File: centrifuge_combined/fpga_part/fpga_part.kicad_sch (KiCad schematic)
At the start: 8 parts, among them X3 EC2620TTS-100.000MTR

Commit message: Board appears ok
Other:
- title: (none) -> VGA Centrifuge
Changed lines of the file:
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@@
 (kicad_sch (version 20211123) (generator eeschema)
   (paper "A4")
+  (title_block
+    (title "VGA Centrifuge")
+    (date "2022-10-03")
+    (rev "R2")
+    (comment 1 "Author: Paolo Celati")
+    (comment 2 "FPGA Section")
+  )
   (junction (at 107.823 154.686) (diameter 0) (color 0 0 0 0)
   )

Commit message: Fixed up schematic names and page numbers
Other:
- sheet e renamed vga_dac
- sheet e1 renamed vga_adc1
- sheet e2 renamed vga_adc2
- sheet e3 renamed vga_ddc_eeprom1
- sheet e4 renamed vga_ddc_eeprom2
- sheet vga_interface renamed vga_interface3
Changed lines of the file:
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@@
     (stroke (width 0.1524) (type solid) (color 0 0 0 0))
     (fill (color 0 0 0 0.0000))
-    (property "Sheet name" "e" (id 0) (at 206.248 43.4844 0)
+    (property "Sheet name" "vga_dac" (id 0) (at 206.248 43.4844 0)
       (effects (font (size 1.27 1.27)) (justify left bottom))
     )
@@
     (stroke (width 0.1524) (type solid) (color 0 0 0 0))
     (fill (color 0 0 0 0.0000))
-    (property "Sheet name" "vga_interface" (id 0) (at 250.063 43.3574 0)
+    (property "Sheet name" "vga_interface3" (id 0) (at 250.063 43.3574 0)
       (effects (font (size 1.27 1.27)) (justify left bottom))
     )
@@
     (stroke (width 0.1524) (type solid) (color 0 0 0 0))
     (fill (color 0 0 0 0.0000))
-    (property "Sheet name" "e1" (id 0) (at 99.441 75.9964 0)
+    (property "Sheet name" "vga_adc1" (id 0) (at 99.441 75.9964 0)
       (effects (font (size 1.27 1.27)) (justify left bottom))
     )
@@
     (stroke (width 0.1524) (type solid) (color 0 0 0 0))
     (fill (color 0 0 0 0.0000))
-    (property "Sheet name" "e3" (id 0) (at 21.463 76.6314 0)
+    (property "Sheet name" "vga_ddc_eeprom1" (id 0) (at 21.463 76.6314 0)
       (effects (font (size 1.27 1.27)) (justify left bottom))
     )
@@
     (stroke (width 0.1524) (type solid) (color 0 0 0 0))
     (fill (color 0 0 0 0.0000))
-    (property "Sheet name" "e2" (id 0) (at 96.393 30.1494 0)
-      (effects (font (size 1.27 1.27)) (justify left bottom))
-    )
-    (property "Sheet file" "vga_input.kicad_sch" (id 1) (at 96.393 48.5906 0)
+    (property "Sheet name" "vga_adc2" (id 0) (at 96.393 30.1494 0)
+      (effects (font (size 1.27 1.27)) (justify left bottom))
+    )
+    (property "Sheet file" "vga_input.kicad_sch" (id 1) (at 96.393 48.7176 0)
       (effects (font (size 1.27 1.27)) (justify left top))
     )
@@
     (stroke (width 0.1524) (type solid) (color 0 0 0 0))
     (fill (color 0 0 0 0.0000))
-    (property "Sheet name" "e4" (id 0) (at 26.543 30.7844 0)
-      (effects (font (size 1.27 1.27)) (justify left bottom))
-    )
+    (property "Sheet name" "vga_ddc_eeprom2" (id 0) (at 26.543 30.7844 0)
+      (effects (font (size 1.27 1.27)) (justify left bottom))
+    )

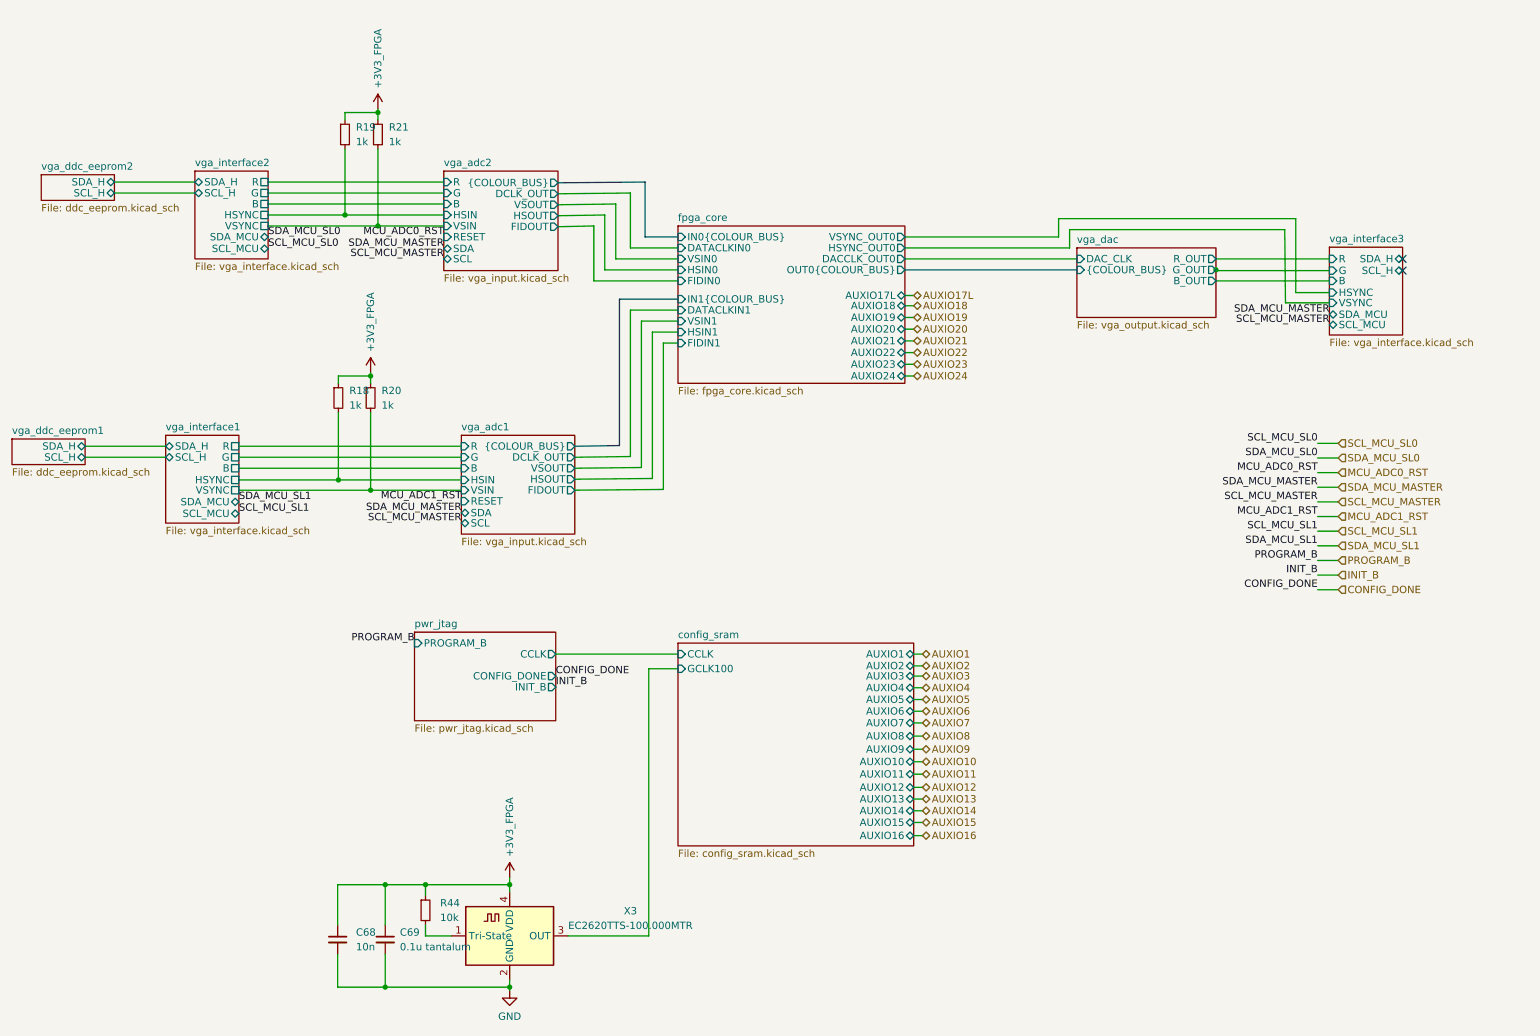
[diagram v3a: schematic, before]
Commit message: fix elprint complaints, except intranet clearance, also widen some traces
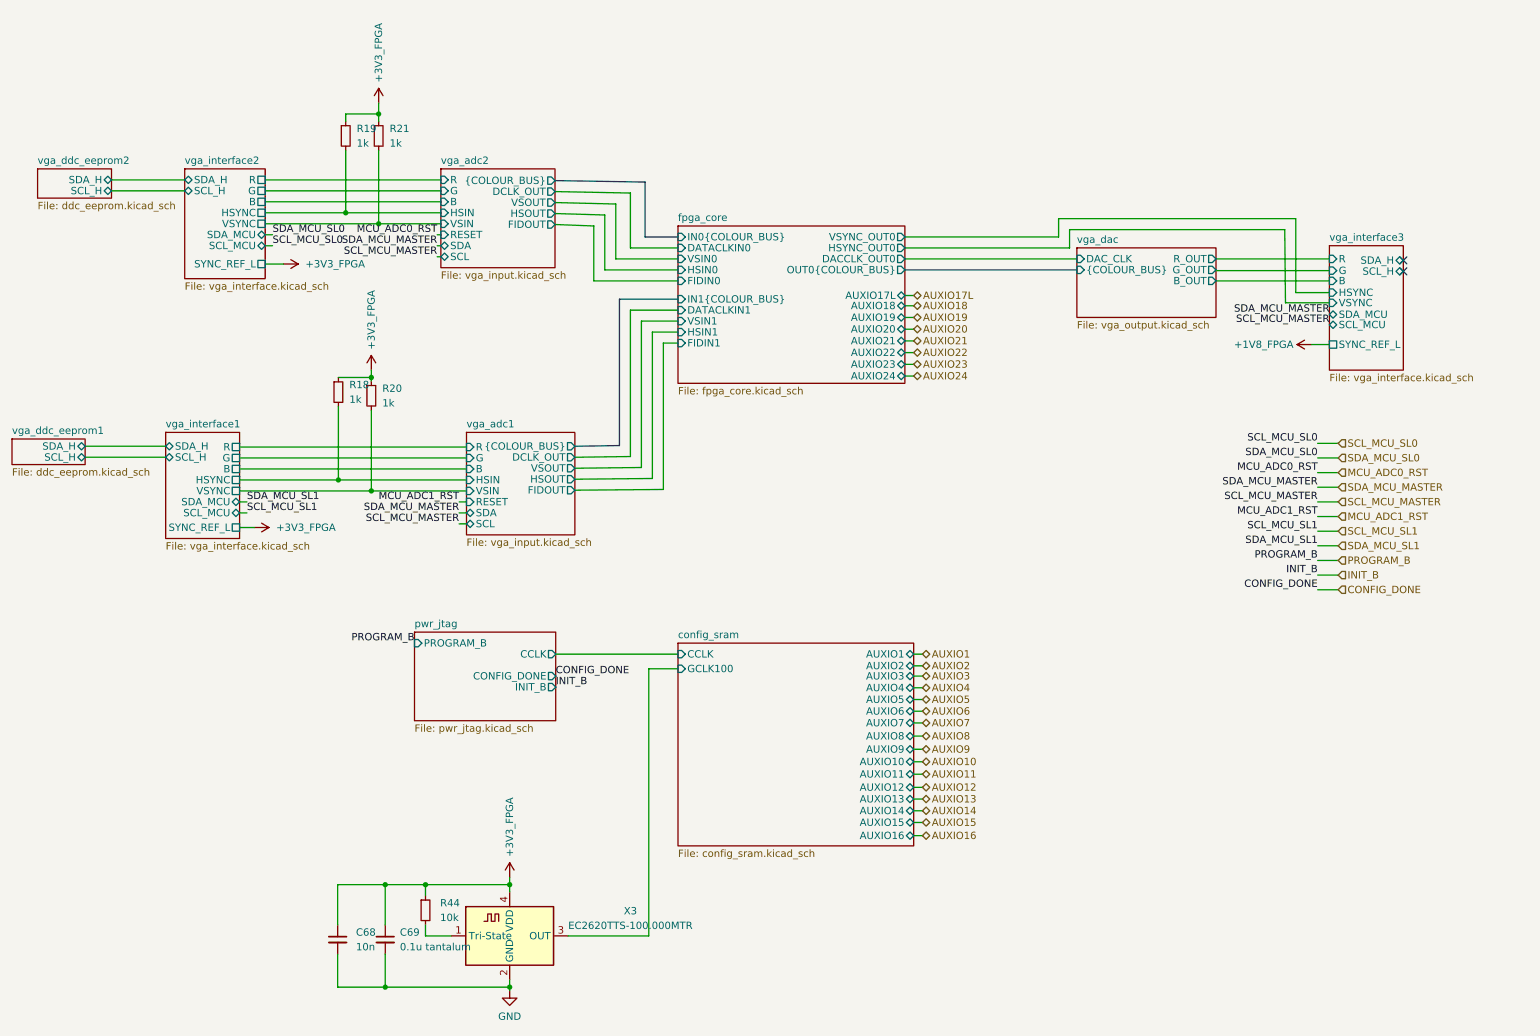
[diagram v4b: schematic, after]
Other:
- sheet vga_interface1 ports: added SYNC_REF_L; removed none
- sheet vga_interface2 ports: added SYNC_REF_L; removed none
- sheet vga_interface3 ports: added SYNC_REF_L; removed none
- moved on the sheet: R18

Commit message: more checks, also make silkscreen text for connectors
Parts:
- X3: Purchase (none) -> TODO
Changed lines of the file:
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@@
+      (effects (font (size 1.27 1.27)) hide)
+    )
+    (property "Purchase" "TODO" (id 4) (at 107.823 163.576 0)
       (effects (font (size 1.27 1.27)) hide)
     )
@@
   (symbol (lib_id "centrifuge_symbols:+3V3_FPGA") (at 68.58 46.99 270) (unit 1)
     (in_bom yes) (on_board yes) (fields_autoplaced)
-    (property "Reference" "#PWR?" (id 0) (at 64.77 46.99 0)
+    (property "Reference" "#PWR0123" (id 0) (at 64.77 46.99 0)
       (effects (font (size 1.27 1.27)) hide)
     )
@@
   (symbol (lib_id "centrifuge_symbols:+3V3_FPGA") (at 63.5 92.71 270) (unit 1)
     (in_bom yes) (on_board yes) (fields_autoplaced)
-    (property "Reference" "#PWR?" (id 0) (at 59.69 92.71 0)
+    (property "Reference" "#PWR0190" (id 0) (at 59.69 92.71 0)
       (effects (font (size 1.27 1.27)) hide)
     )

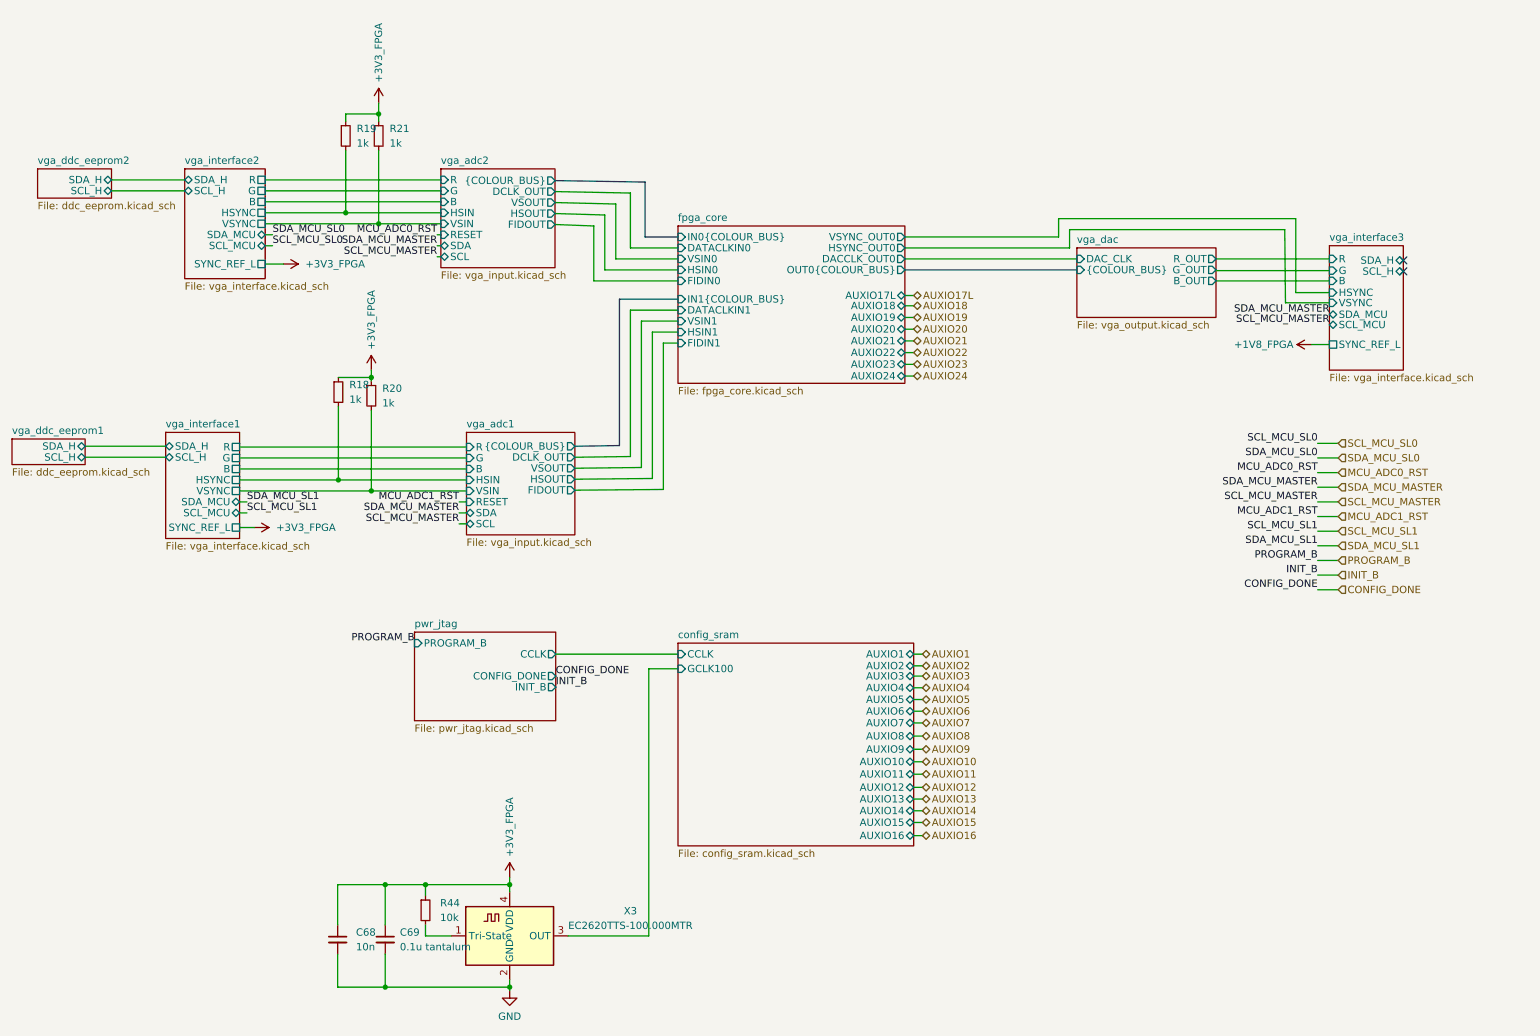
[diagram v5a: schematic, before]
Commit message: Fixed Elprint complaints and JTAG VREF problems+config flash CS
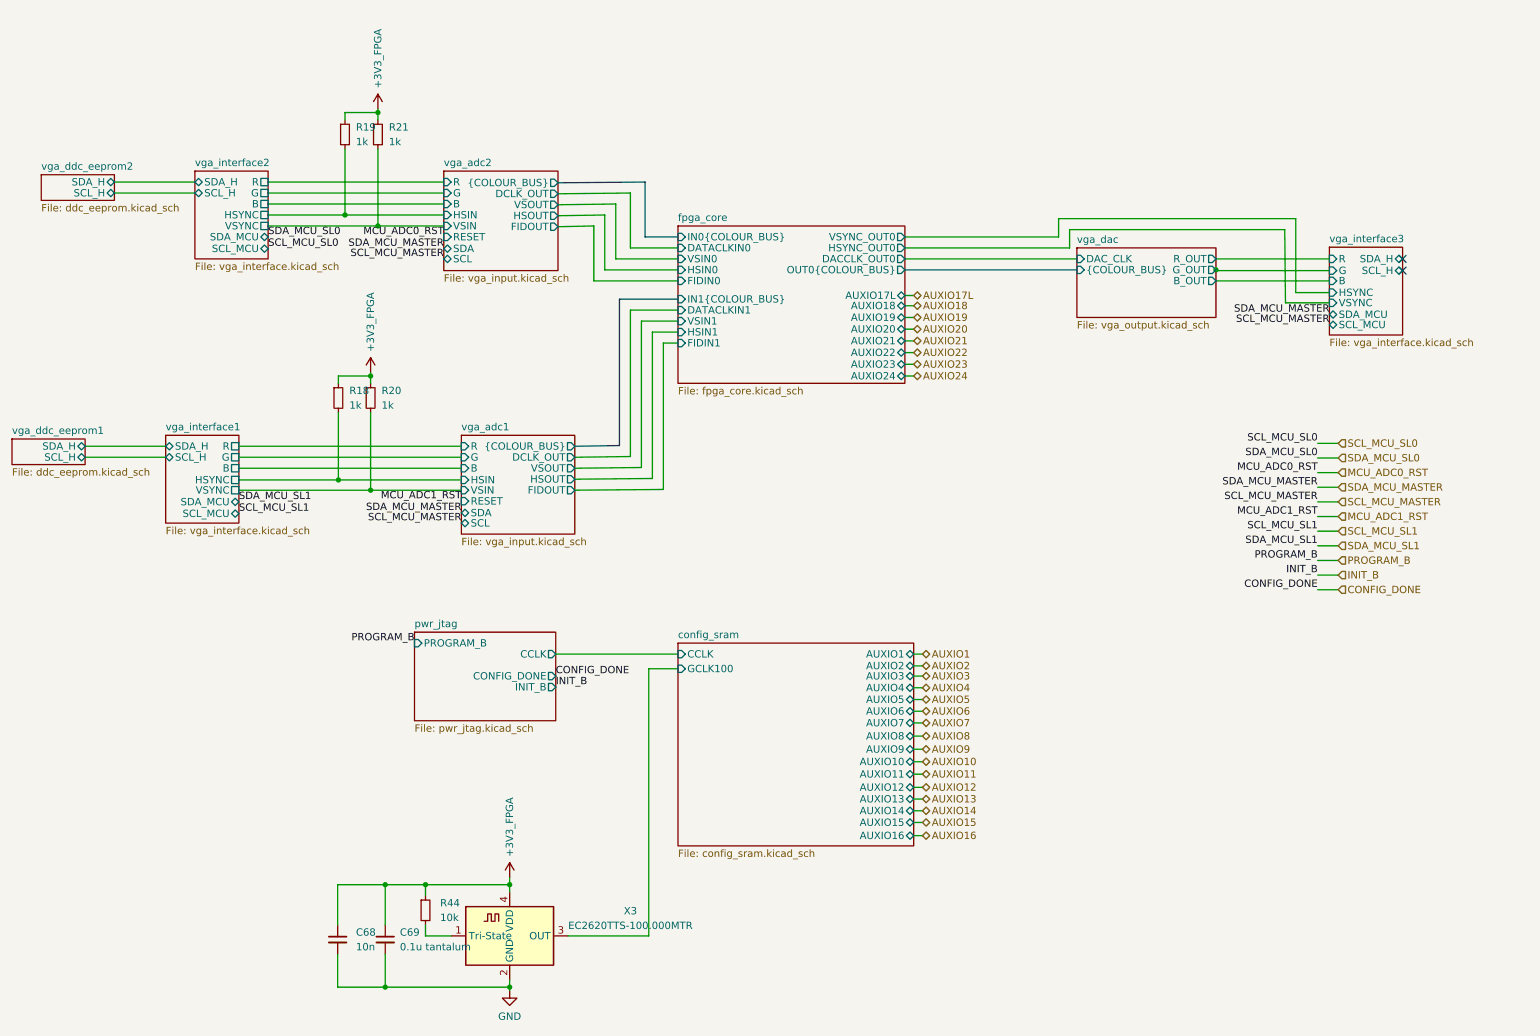
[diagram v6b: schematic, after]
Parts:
- X3: Purchase TODO -> (none)
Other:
- sheet vga_interface1 ports: added none; removed SYNC_REF_L
- sheet vga_interface2 ports: added none; removed SYNC_REF_L
- sheet vga_interface3 ports: added none; removed SYNC_REF_L
- moved on the sheet: R18
